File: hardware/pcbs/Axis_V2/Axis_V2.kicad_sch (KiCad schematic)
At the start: 33 parts, among them J1 SWD, J2 UART, J3 Conn_01x02, J4 Conn_01x02, J5 Conn_01x04, J6 Conn_01x10, J7 Conn_01x08, SW1 RES, U1 Pico, U2 MAX31855EASA, U3 MAX31855EASA, U4 MAX6107, U5 FM24CL16B, U6 ADS1119IPWR, U7 TCA9534, U9 DS3231MZ

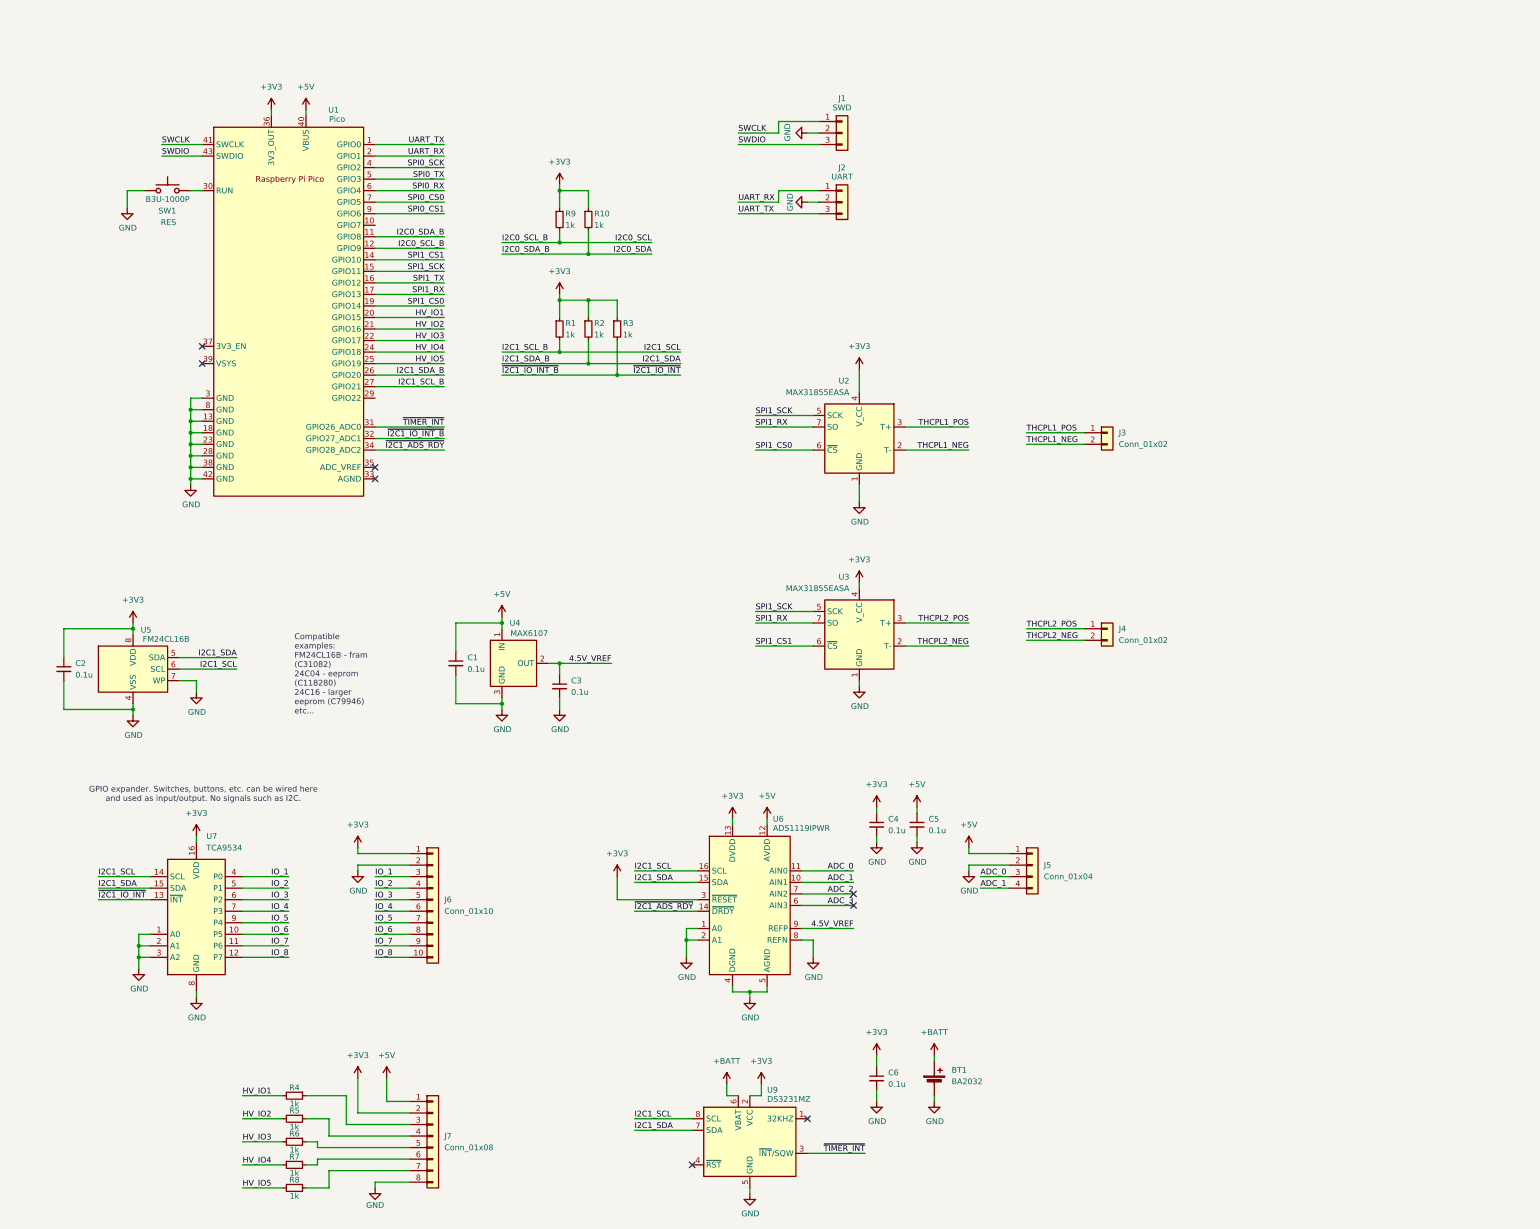
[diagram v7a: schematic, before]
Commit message: Added a I2C expander for non-essential peripherals, etc.
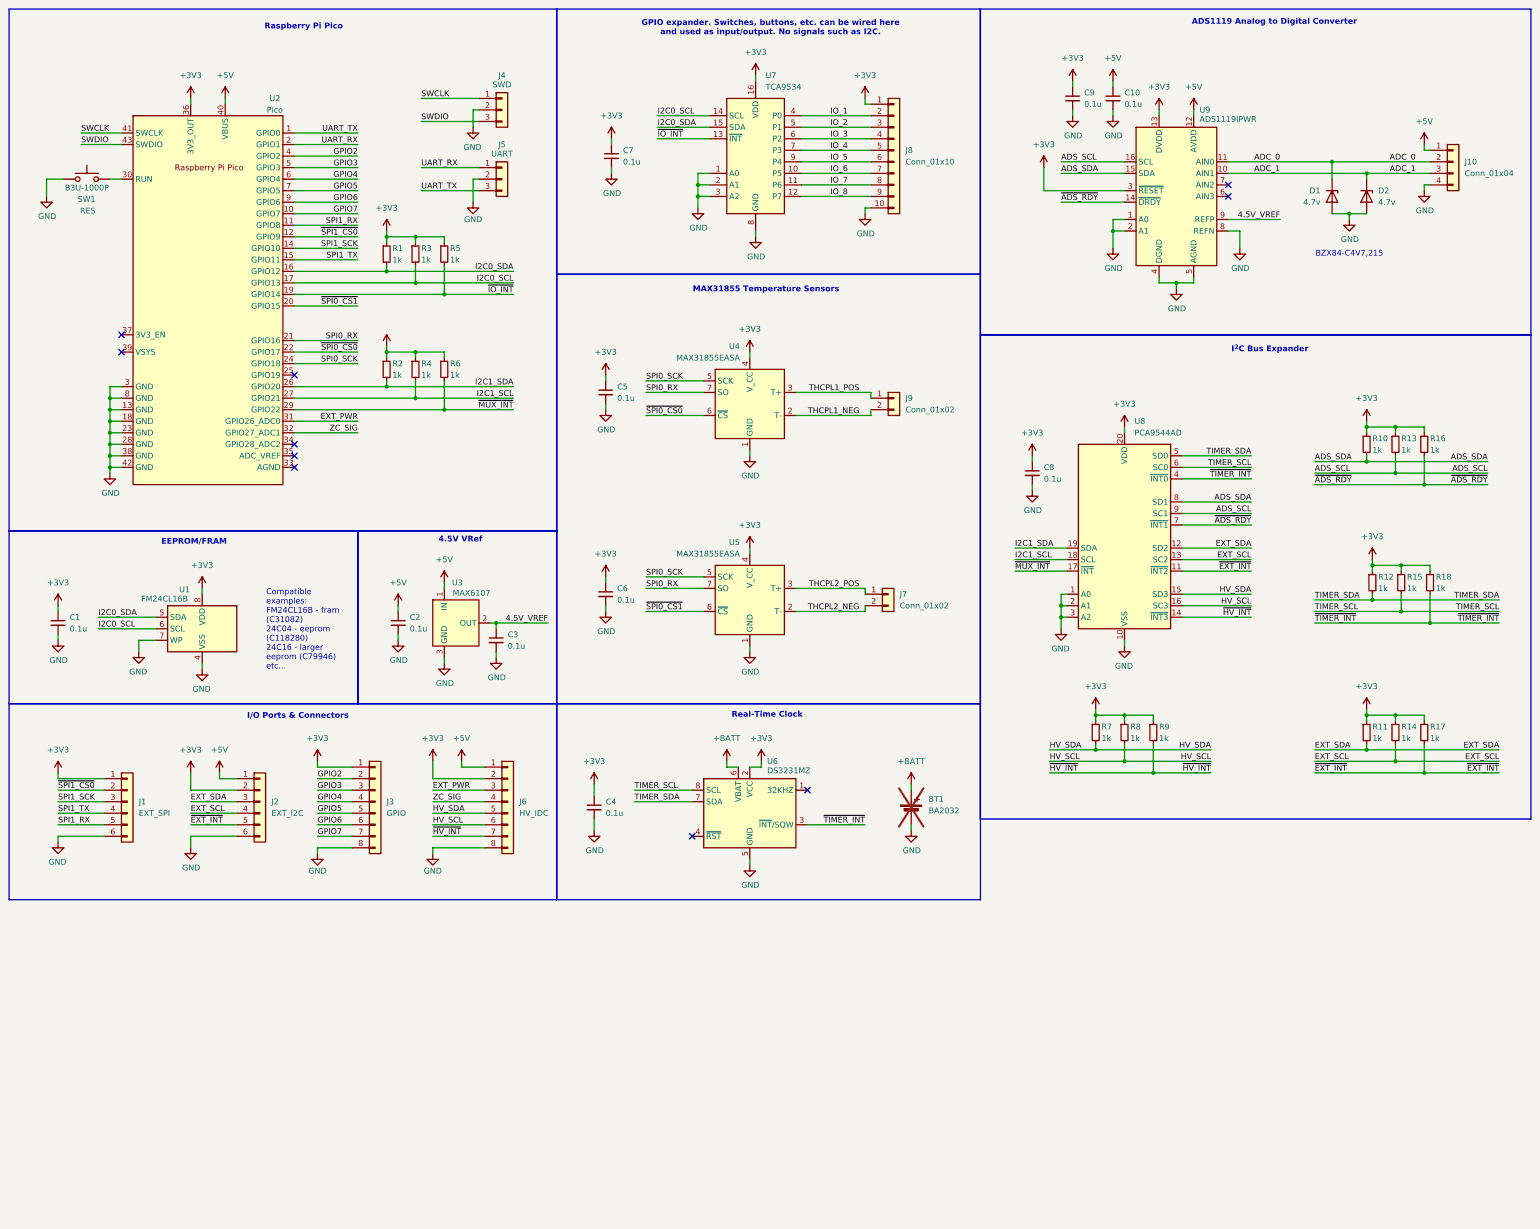
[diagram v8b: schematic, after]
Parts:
- removed U1: Pico, MCU_RaspberryPi_and_Boards:RPi_Pico_SMD_TH, symbol Project_Library:Pico
- added C5, C6, C7, C8: 0.1u, Capacitor_SMD:C_0603_1608Metric_Pad1.08x0.95mm_HandSolder, symbol Device:C_Small
- added D1, D2: 4.7v, Package_TO_SOT_SMD:SOT-23, symbol Device:D_Zener
- added J1: EXT_SPI, Connector_PinSocket_2.54mm:PinSocket_1x06_P2.54mm_Vertical, symbol Connector_Generic:Conn_01x06
- added J2: EXT_I2C, Connector_PinSocket_2.54mm:PinSocket_1x06_P2.54mm_Vertical, symbol Connector_Generic:Conn_01x06
- added J3: GPIO, Connector_PinSocket_2.54mm:PinSocket_1x08_P2.54mm_Vertical, symbol Connector_Generic:Conn_01x08
- added R11, R12, R13, R14, R15, R16, R17, R18: 1k, Resistor_SMD:R_0603_1608Metric_Pad0.98x0.95mm_HandSolder, symbol Device:R_Small
- added U2: Pico, MCU_RaspberryPi_and_Boards:RPi_Pico_SMD_TH, symbol Project_Library:Pico
- added U8: PCA9544AD, Package_SO:SOIC-20W_7.5x12.8mm_P1.27mm, symbol Interface_Expansion:PCA9544AD
- BT1: now not fitted
- C1, C2, C3: footprint Capacitor_SMD:C_0402_1005Metric_Pad0.74x0.62mm_HandSolder -> Capacitor_SMD:C_0603_1608Metric_Pad1.08x0.95mm_HandSolder
- C10: renamed from C5; footprint Capacitor_SMD:C_0402_1005Metric_Pad0.74x0.62mm_HandSolder -> Capacitor_SMD:C_0603_1608Metric_Pad1.08x0.95mm_HandSolder
- C4: renamed from C6; footprint Capacitor_SMD:C_0402_1005Metric_Pad0.74x0.62mm_HandSolder -> Capacitor_SMD:C_0603_1608Metric_Pad1.08x0.95mm_HandSolder
- C9: renamed from C4; footprint Capacitor_SMD:C_0402_1005Metric_Pad0.74x0.62mm_HandSolder -> Capacitor_SMD:C_0603_1608Metric_Pad1.08x0.95mm_HandSolder
- J6: renamed from J7; value Conn_01x08 -> HV_IDC
- R1, R10, R2, R3, R4, R5, R6, R7, R8, R9: footprint Resistor_SMD:R_0402_1005Metric_Pad0.72x0.64mm_HandSolder -> Resistor_SMD:R_0603_1608Metric_Pad0.98x0.95mm_HandSolder
- U7: footprint Package_SO:SOIC-16W_7.5x10.3mm_P1.27mm -> Package_SO:TSSOP-16_4.4x5mm_P0.65mm
- renumbered J5 to J10, J1 to J4, J2 to J5, J4 to J7, J6 to J8, J3 to J9, U5 to U1, U4 to U3, U2 to U4, U3 to U5, U9 to U6, U6 to U9
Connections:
- net HV_IO1 is gone; now on net I2C1_SCL: R4.2
- net HV_IO4 is gone; now on net HV_SDA: R7.2
- net HV_IO5 is gone; now on net HV_SCL: R8.2
- net +3V3: now also C1.1, R4.1, R5.1, R6.1, R7.1, R8.1, C5.1, C6.1, C7.1, C8.1, J1.1 (Pin_1), J2.2 (Pin_2), J3.1 (Pin_1), R11.1, R12.1, R13.1, R14.1, R15.1, R16.1, R17.1, R18.1, U2.36 (3V3_OUT), U8.20 (VDD); no longer C2.1
- net +5V: now also C2.1, J2.1 (Pin_1), U2.40 (VBUS); no longer C1.1
- net ADC_0: now also J10.2 (Pin_2), D1.1 (K); no longer J10.3 (Pin_3)
- net ADC_1: now also J10.3 (Pin_3), D2.1 (K); no longer J10.4 (Pin_4)
- net GND: now also J10.4 (Pin_4), J8.10 (Pin_10), C5.2, C6.2, C7.2, C8.2, D1.2 (A), D2.2 (A), J1.6 (Pin_6), J2.6 (Pin_6), J3.8 (Pin_8), U2.13 (GND), U2.18 (GND), U2.23 (GND), U2.28 (GND), U2.3 (GND), U2.38 (GND), U2.42 (GND), U2.8 (GND), U8.1 (A0), U8.10 (VSS), U8.2 (A1), U8.3 (A2); no longer J10.2 (Pin_2), J8.2 (Pin_2)
- net I2C0_SCL: now also R3.2, U1.6 (SCL), U7.14 (SCL), U2.17 (GPIO13); no longer R9.2
- net I2C0_SDA: now also R1.2, U1.5 (SDA), U7.15 (SDA), U2.16 (GPIO12); no longer R10.2
- net I2C1_SCL: now also U2.27 (GPIO21), U8.18 (SCL); no longer R1.2, U1.6 (SCL), U6.8 (SCL), U7.14 (SCL), U9.16 (SCL)
- net I2C1_SDA: now also U2.26 (GPIO20), U8.19 (SDA); no longer U1.5 (SDA), U6.7 (SDA), U7.15 (SDA), U9.15 (SDA)
- net IO_1: now also J8.2 (Pin_2); no longer J8.3 (Pin_3)
- net IO_2: now also J8.3 (Pin_3); no longer J8.4 (Pin_4)
- net IO_3: now also J8.4 (Pin_4); no longer J8.5 (Pin_5)
- net IO_4: now also J8.5 (Pin_5); no longer J8.6 (Pin_6)
- net IO_5: now also J8.6 (Pin_6); no longer J8.7 (Pin_7)
- net IO_6: now also J8.7 (Pin_7); no longer J8.8 (Pin_8)
- net IO_7: now also J8.8 (Pin_8); no longer J8.9 (Pin_9)
- net IO_8: now also J8.9 (Pin_9); no longer J8.10 (Pin_10)
- net SPI0_RX: now also U4.7 (SO), U5.7 (SO), U2.21 (GPIO16)
- net SPI0_SCK: now also U4.5 (SCK), U5.5 (SCK), U2.24 (GPIO18)
- net SPI1_RX: now also J1.5 (Pin_5), U2.11 (GPIO8); no longer U4.7 (SO), U5.7 (SO)
- net SPI1_SCK: now also J1.3 (Pin_3), U2.14 (GPIO10); no longer U4.5 (SCK), U5.5 (SCK)
- net SPI1_TX: now also J1.4 (Pin_4), U2.15 (GPIO11)
- net SWCLK: now also U2.41 (SWCLK)
- net SWDIO: now also U2.43 (SWDIO)
- net UART_RX: now also U2.2 (GPIO1)
- net UART_TX: now also U2.1 (GPIO0)
- net ~{TIMER_INT}: now also R18.2, U8.4 (~{INT0})
- net EXT_PWR: now reaches J6.3 (Pin_3)
- net EXT_PWR: now also U2.31 (GPIO26_ADC0); no longer R4.1
- net HV_SCL: now reaches J6.6 (Pin_6)
- net HV_SCL: now also U8.16 (SC3); no longer R7.1
- net at SW1.2: now also U2.30 (RUN)
- net ~{HV_INT}: now reaches J6.7 (Pin_7)
- net ~{HV_INT}: now also R9.2, U8.14 (~{INT3}); no longer R8.1
- net HV_SDA: now reaches J6.5 (Pin_5)
- net HV_SDA: now also U8.15 (SD3); no longer R6.1
- net ZC_SIG: now reaches J6.4 (Pin_4)
- net ZC_SIG: now also U2.32 (GPIO27_ADC1); no longer R5.1
- net ADC_2: no longer names the net of U9.7 (AIN2)
- net ADC_3: no longer names the net of U9.6 (AIN3)
- net HV_IO2 renamed ~{IO_INT}
- net ~{IO_INT}: now also U7.13 (~{INT}), U2.19 (GPIO14)
- net HV_IO3 renamed ~{MUX_INT}
- net ~{MUX_INT}: now also U2.29 (GPIO22), U8.17 (~{INT})
- net SPI1_CS0 renamed ~{SPI0_CS0}
- net ~{SPI0_CS0}: now also U2.22 (GPIO17)
- net SPI1_CS1 renamed ~{SPI0_CS1}
- net ~{SPI0_CS1}: now also U2.20 (GPIO15)
- net ~{I2C1_ADS_RDY} renamed ~{ADS_RDY}
- net ~{ADS_RDY}: now also R16.2, U8.7 (~{INT1})
- removed net ~{I2C1_IO_INT_B}: R3.2, U7.13 (~{INT})
- new net ADS_SCL: R13.2, U8.9 (SC1), U9.16 (SCL)
- new net ADS_SDA: R10.2, U8.8 (SD1), U9.15 (SDA)
- new net EXT_SCL: J2.4 (Pin_4), R14.2, U8.13 (SC2)
- new net EXT_SDA: J2.3 (Pin_3), R11.2, U8.12 (SD2)
- new net GPIO2: J3.2 (Pin_2), U2.4 (GPIO2)
- new net GPIO3: J3.3 (Pin_3), U2.5 (GPIO3)
- new net GPIO4: J3.4 (Pin_4), U2.6 (GPIO4)
- new net GPIO5: J3.5 (Pin_5), U2.7 (GPIO5)
- new net GPIO6: J3.6 (Pin_6), U2.9 (GPIO6)
- new net GPIO7: J3.7 (Pin_7), U2.10 (GPIO7)
- new net TIMER_SCL: R15.2, U6.8 (SCL), U8.6 (SC0)
- new net TIMER_SDA: R12.2, U6.7 (SDA), U8.5 (SD0)
- new net ~{EXT_INT}: J2.5 (Pin_5), R17.2, U8.11 (~{INT2})
- new net ~{SPI1_CS0}: J1.2 (Pin_2), U2.12 (GPIO9)
- no-connect marks 8 -> 10
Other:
- note added: "4.5V VRef"
- note added: "ADS1119 Analog to Digital Converter"
- note added: "BZX84-C4V7,215"
- note added: "EEPROM/FRAM"
- note added: "I/O Ports & Connectors"
- note added: "I^{2}C Bus Expander"
- note added: "MAX31855 Temperature Sensors"
- note added: "Raspberry Pi Pico"
- note added: "Real-Time Clock"
- title: (none) -> Axis Control PCB
- moved on the sheet: C10, C3, C4, C9, J10, J4, J5, J6, J7, J8, J9, SW1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
